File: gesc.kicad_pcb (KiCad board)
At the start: 4 copper layers, 111 x 111 mm, 164 parts, among them J1 Conn_01x06, J10 PHASE_C, J11 PHASE_B, J12 NTC, J13 T-Motor, J14 Conn_01x03, J15 EXT_OFF, J2 Conn_01x06, J3 Conn_01x06, J4 Conn_01x05, J5 Conn_01x03, J6 USB_B_Mini, J7 BAT+, J8 BAT-, J9 PHASE_A, Q1 BSC070N10NS5, Q2 BSC070N10NS5, Q3 BSC070N10NS5, Q4 BSC070N10NS5, Q5 BSC070N10NS5, Q6 BSC070N10NS5, U1 STM32F405RGTx, U10 LM5008MM, U11 SN74LVC1G66DBVR, U12 LM5107, U13 SN74LVC1G66DBVR, U14 AQY282S, U15 LM5107, U16 EYSGJNZWY, U17 LMR12010YMKE_NOPB, U2 SN74LVC1G66DBVR, U3 LM5107, U4 INA240A1, U5 INA240A1, U6 INA240A1, U7 SN74LVC1G66DBVR, U8 SN74LVC1G66DBVR, U9 SN74LVC1G66DBVR, Y1 X50328MSB2GI

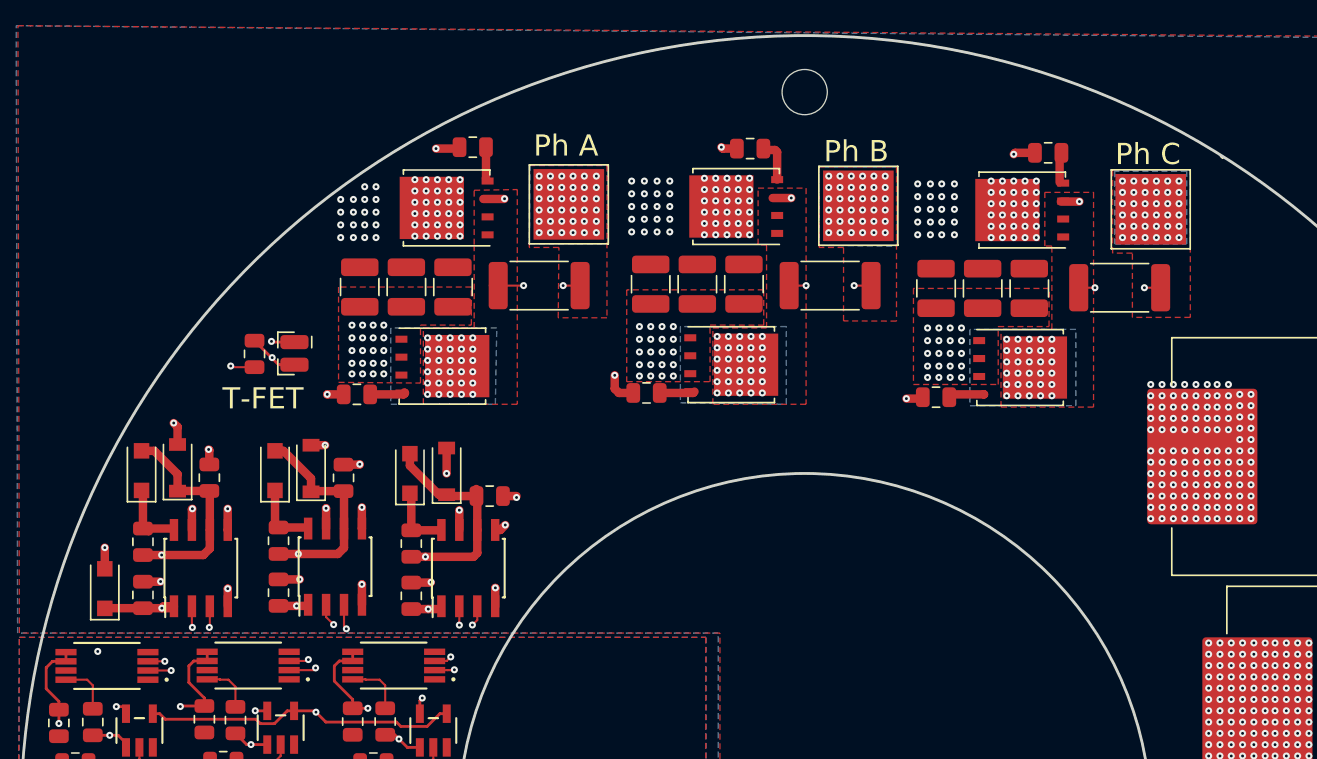
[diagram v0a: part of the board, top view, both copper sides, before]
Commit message: Version mit UCC27211
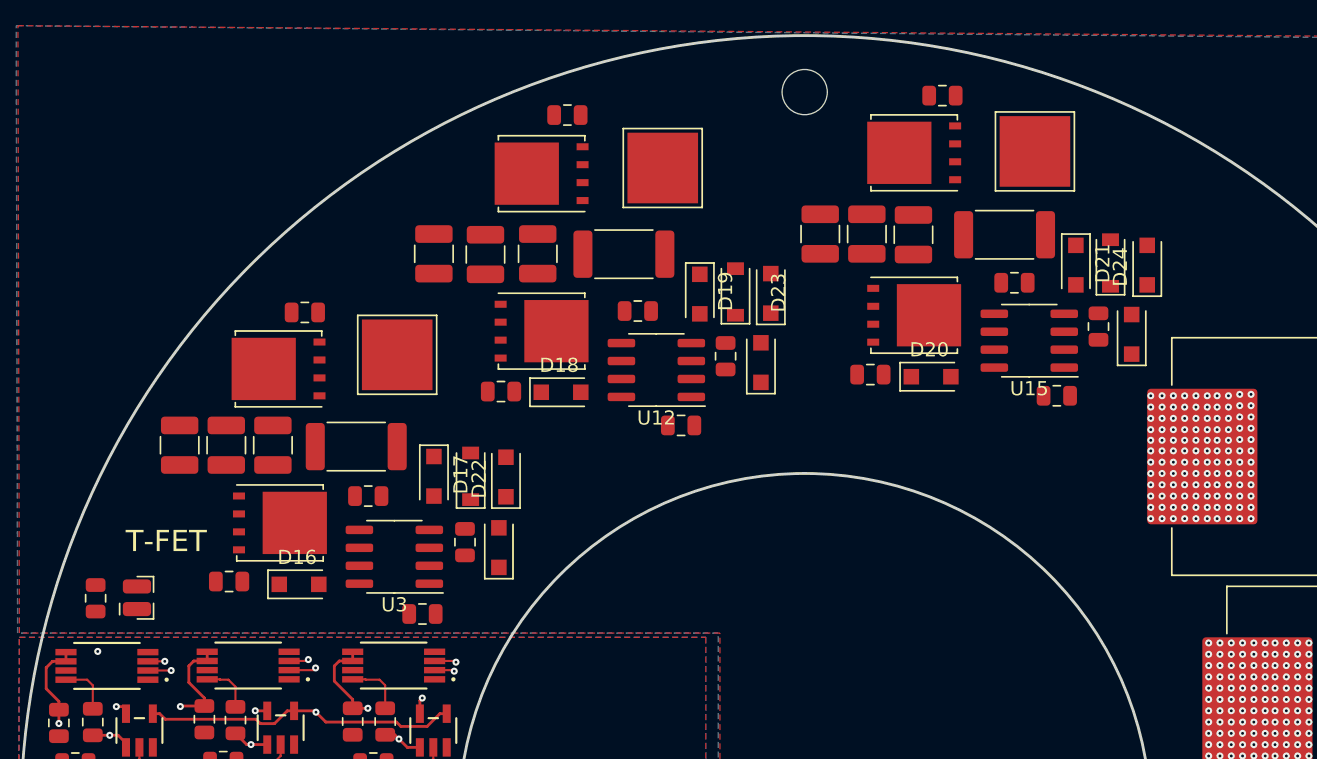
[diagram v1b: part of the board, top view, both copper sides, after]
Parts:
- added D17: SMF14A, Diode_SMD:D_SOD-123F, F.Cu at (73.7, 75.7)
- added D18: SMF14A, Diode_SMD:D_SOD-123F, F.Cu at (82.7, 69.7)
- added D19: SMF14A, Diode_SMD:D_SOD-123F, F.Cu at (92.6, 62.8)
- added D20: SMF14A, Diode_SMD:D_SOD-123F, F.Cu at (108.9, 68.6)
- added D21: SMF14A, Diode_SMD:D_SOD-123F, F.Cu at (119.2, 60.7)
- added D22: SMF58A, Diode_SMD:D_SOD-123F, F.Cu at (78.8, 75.7)
- added D23: SMF58A, Diode_SMD:D_SOD-123F, F.Cu at (97.6, 62.7)
- added D24: SMF58A, Diode_SMD:D_SOD-123F, F.Cu at (124.2, 60.7)
- D16: value SMF12A -> SMF14A
- U12, U15, U3: value LM5107 -> UCC27211
- moved D15 52.0 mm to (123.1, 65.6)
- moved C32 51.0 mm to (120.8, 65.1), turned to 90 degrees
- moved D12 49.3 mm to (121.6, 60.6)
- moved C29 47.8 mm to (117.8, 70.0), turned to 180 degrees
- moved U15 42.9 mm to (115.9, 66.1), turned to 180 degrees
- moved R49 40.1 mm to (114.8, 62.0), turned to 0 degrees
- moved D14 35.2 mm to (96.9, 67.6)
- moved C27 34.2 mm to (94.4, 67.2), turned to 90 degrees
- moved D10 32.5 mm to (95.1, 62.6)
- moved C22 30.9 mm to (91.2, 72.1), turned to 180 degrees
- moved U12 26.7 mm to (89.5, 68.2), turned to 180 degrees
- moved D13 25.9 mm to (78.3, 80.7)
- moved R48 24.0 mm to (88.2, 64.0), turned to 0 degrees
- moved C21 22.8 mm to (75.9, 80.4), turned to 90 degrees
- moved C38 22.1 mm to (73.7, 59.9)
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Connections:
- D16 pad 1: +12V -> /Driver/GL_A
- R13 pad 1: /Driver/SH_A_R -> /Driver/SH_A
- R17 pad 1: /Driver/SH_B_R -> /Driver/SH_B
- R19 pad 1: /Driver/SH_C_R -> /Driver/SH_C
- U12 pad 2: /MCU/H2 -> Net-(C27-Pad1)
- U12 pad 3: /MCU/L2 -> /Driver/GH_B
- U12 pad 4: GND -> /Driver/SH_B_R
- U12 pad 5: /Driver/GL_B -> /MCU/H2
- U12 pad 6: /Driver/SH_B_R -> /MCU/L2
- U12 pad 7: /Driver/GH_B -> GND
- U12 pad 8: Net-(C27-Pad1) -> /Driver/GL_B
- U15 pad 2: /MCU/H3 -> Net-(C32-Pad1)
- U15 pad 3: /MCU/L3 -> /Driver/GH_C
- U15 pad 4: GND -> /Driver/SH_C_R
- U15 pad 5: /Driver/GL_C -> /MCU/H3
- U15 pad 6: /Driver/SH_C_R -> /MCU/L3
- U15 pad 7: /Driver/GH_C -> GND
- U15 pad 8: Net-(C32-Pad1) -> /Driver/GL_C
- U3 pad 2: /MCU/H1 -> Net-(C21-Pad1)
- U3 pad 3: /MCU/L1 -> /Driver/GH_A
- U3 pad 4: GND -> /Driver/SH_A_R
- U3 pad 5: /Driver/GL_A -> /MCU/H1
- U3 pad 6: /Driver/SH_A_R -> /MCU/L1
- U3 pad 7: /Driver/GH_A -> GND
- U3 pad 8: Net-(C21-Pad1) -> /Driver/GL_A
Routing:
- net GND: track 117.4 -> 0.74 mm, vias 390 -> 319
- net /Driver/SH_B: track 104.3 -> 23.6 mm, vias 34 -> 2
- net /Driver/SH_C: track 122.9 -> 46.1 mm, vias 34 -> 2
- net /Driver/SH_A: track 86.7 -> 17.1 mm, vias 34 -> 2
- net /Driver/GH_C: track 56.1 -> 0.00 mm, vias 2 -> 0
- net /POWER/PHASE_B: track 59.0 -> 9.98 mm, vias 38 -> 1
- net /Driver/GH_B: track 45.1 -> 0.00 mm, vias 2 -> 0
- net /POWER/PHASE_A: track 49.5 -> 6.33 mm, vias 38 -> 1
- net /Driver/GH_A: track 36.6 -> 0.00 mm, vias 2 -> 0
- net /POWER/PHASE_C: track 67.0 -> 30.5 mm, vias 38 -> 1
- net /Driver/SH_A_R: track 36.1 -> 0.00 mm, vias 2 -> 0
- net /Driver/SH_B_R: track 35.4 -> 0.00 mm, vias 2 -> 0
- net /Driver/SH_C_R: track 35.3 -> 0.00 mm, vias 2 -> 0
- net /Driver/GL_C: track 34.9 -> 0.00 mm, vias 2 -> 0
- net /MCU/H3: track 27.9 -> 62.2 mm, vias 2 -> 1
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- removed copper zone on B.Cu, net /Driver/SH_A
- removed copper zone on F.Cu, net /Driver/SH_A
- removed copper zone on B.Cu, net /Driver/SH_B
- removed copper zone on F.Cu, net /Driver/SH_B
- removed copper zone on B.Cu, net /Driver/SH_C
- removed copper zone on F.Cu, net /Driver/SH_C
- removed copper zone on B.Cu, net /POWER/PHASE_A
- removed copper zone on F.Cu, net /POWER/PHASE_A
- removed copper zone on B.Cu, net /POWER/PHASE_B
- removed copper zone on F.Cu, net /POWER/PHASE_B
- removed copper zone on B.Cu, net /POWER/PHASE_C
- removed copper zone on F.Cu, net /POWER/PHASE_C
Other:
- net class POWER: trace_width 0.2 -> 0.6
- rule trace_min: 0.1 -> 0.15
- board text removed: "Ph A"
- board text removed: "Ph B"
- board text removed: "Ph C"

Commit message: save
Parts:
- removed D10, D12, D9: MBR2H100SFTN, Diode_SMD:D_SOD-123
- removed D13, D14, D15, D16, D17, D18, D19, D20, D21: SMF14A, Diode_SMD:D_SOD-123F
- removed D22, D23, D24: SMF58A, Diode_SMD:D_SOD-123F
- removed R47, R48, R49: 5r60, Resistor_SMD:R_0805_2012Metric
- U12, U15, U3: value UCC27211 -> 2ED2304S06F
- moved C15 4.48 mm to (68.7, 83.9)
- moved C29 3.31 mm to (114.6, 70.5)
- moved R43 3.17 mm to (81.6, 70.3)
- moved C22 2.58 mm to (89.3, 70.3)
- moved U12 2.53 mm to (91.3, 66.4), turned to 0 degrees
- moved C27 2.51 mm to (96.2, 65.5), turned to 270 degrees
- moved J11 2.30 mm to (92.0, 54.8)
- moved Q5 2.30 mm to (83.5, 55.2)
- moved R42 2.30 mm to (85.3, 51.1)
- moved C38 2.30 mm to (75.8, 60.9)
- moved R46 2.30 mm to (89.3, 60.9)
- moved Q6 2.30 mm to (83.5, 66.4)
- moved C44 2.30 mm to (79.5, 60.9)
- moved C53 2.30 mm to (83.2, 60.9)
- moved R26 2.29 mm to (106.2, 70.2)
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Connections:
- C21 pad 2: /Driver/SH_A_R -> /Driver/SH_A
- C27 pad 2: /Driver/SH_B_R -> /Driver/SH_B
- C32 pad 2: /Driver/SH_C_R -> /Driver/SH_C
- U12 pad 1: +12V -> /MCU/L2
- U12 pad 2: Net-(C27-Pad1) -> /MCU/H2
- U12 pad 3: /Driver/GH_B -> +12V
- U12 pad 4: /Driver/SH_B_R -> GND
- U12 pad 5: /MCU/H2 -> /Driver/GL_B
- U12 pad 6: /MCU/L2 -> /Driver/SH_B
- U12 pad 7: GND -> /Driver/GH_B
- U12 pad 8: /Driver/GL_B -> Net-(C27-Pad1)
- U15 pad 1: +12V -> /MCU/L3
- U15 pad 2: Net-(C32-Pad1) -> /MCU/H3
- U15 pad 3: /Driver/GH_C -> +12V
- U15 pad 4: /Driver/SH_C_R -> GND
- U15 pad 5: /MCU/H3 -> /Driver/GL_C
- U15 pad 6: /MCU/L3 -> /Driver/SH_C
- U15 pad 7: GND -> /Driver/GH_C
- U15 pad 8: /Driver/GL_C -> Net-(C32-Pad1)
- U3 pad 1: +12V -> /MCU/L1
- U3 pad 2: Net-(C21-Pad1) -> /MCU/H1
- U3 pad 3: /Driver/GH_A -> +12V
- U3 pad 4: /Driver/SH_A_R -> GND
- U3 pad 5: /MCU/H1 -> /Driver/GL_A
- U3 pad 6: /MCU/L1 -> /Driver/SH_A
- U3 pad 7: GND -> /Driver/GH_A
- U3 pad 8: /Driver/GL_A -> Net-(C21-Pad1)
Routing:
- net /Driver/SH_C: track 46.1 -> 97.0 mm, vias 2 -> 41
- net /POWER/PHASE_C: track 30.5 -> 58.4 mm, vias 1 -> 51
- net /Driver/GH_C: track 0.00 -> 25.5 mm, vias 0 -> 2
- net /MCU/L3: track 65.5 -> 83.9 mm, vias 1 -> 2
- net /MCU/H3: track 62.2 -> 79.6 mm, vias 1 -> 2
- net /Driver/GL_C: track 0.00 -> 13.0 mm, vias 0 -> 2
- net GND: track 0.74 -> 13.3 mm, vias 319 -> 375
- net +12V: track 126.8 -> 131.3 mm
- net /Driver/SH_A: track 17.1 -> 19.8 mm
- net Net-(C32-Pad1): track 0.00 -> 2.58 mm
- net Net-(Q4-Pad4): track 0.00 -> 2.14 mm
- net Net-(Q3-Pad4): track 0.00 -> 2.14 mm
- net VBAT: vias 318 -> 389
- added copper zone on F.Cu, net /Driver/SH_C
- added copper zone on F.Cu, net /POWER/PHASE_C

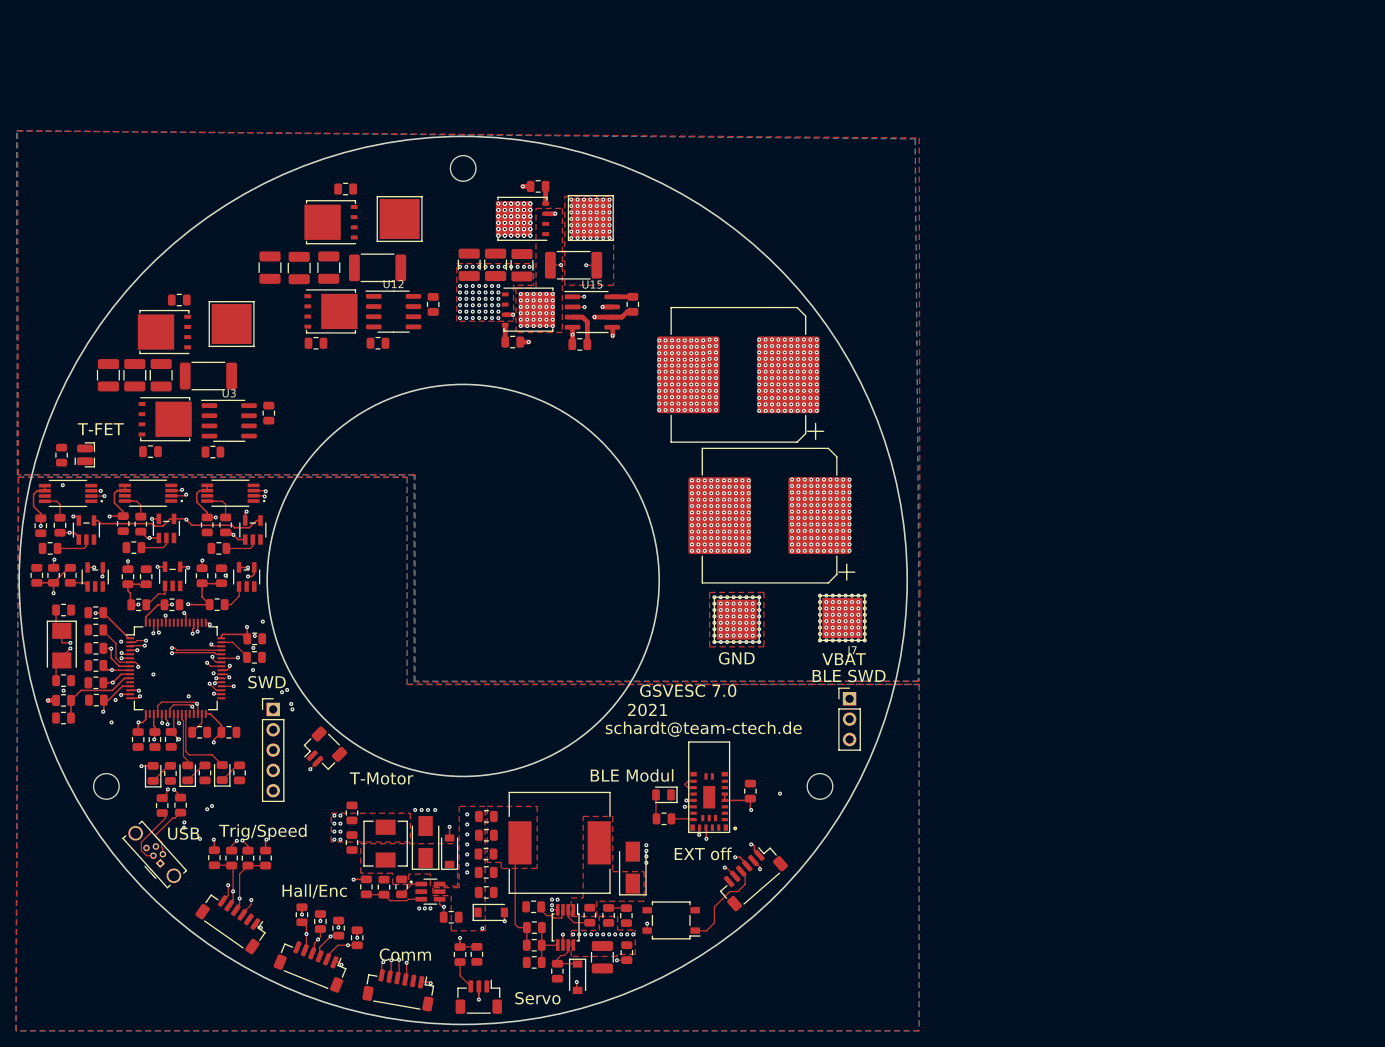
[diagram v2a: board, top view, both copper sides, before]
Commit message: - new driver 2ED2304S06F - separat Elkos for each phase - new FET placement
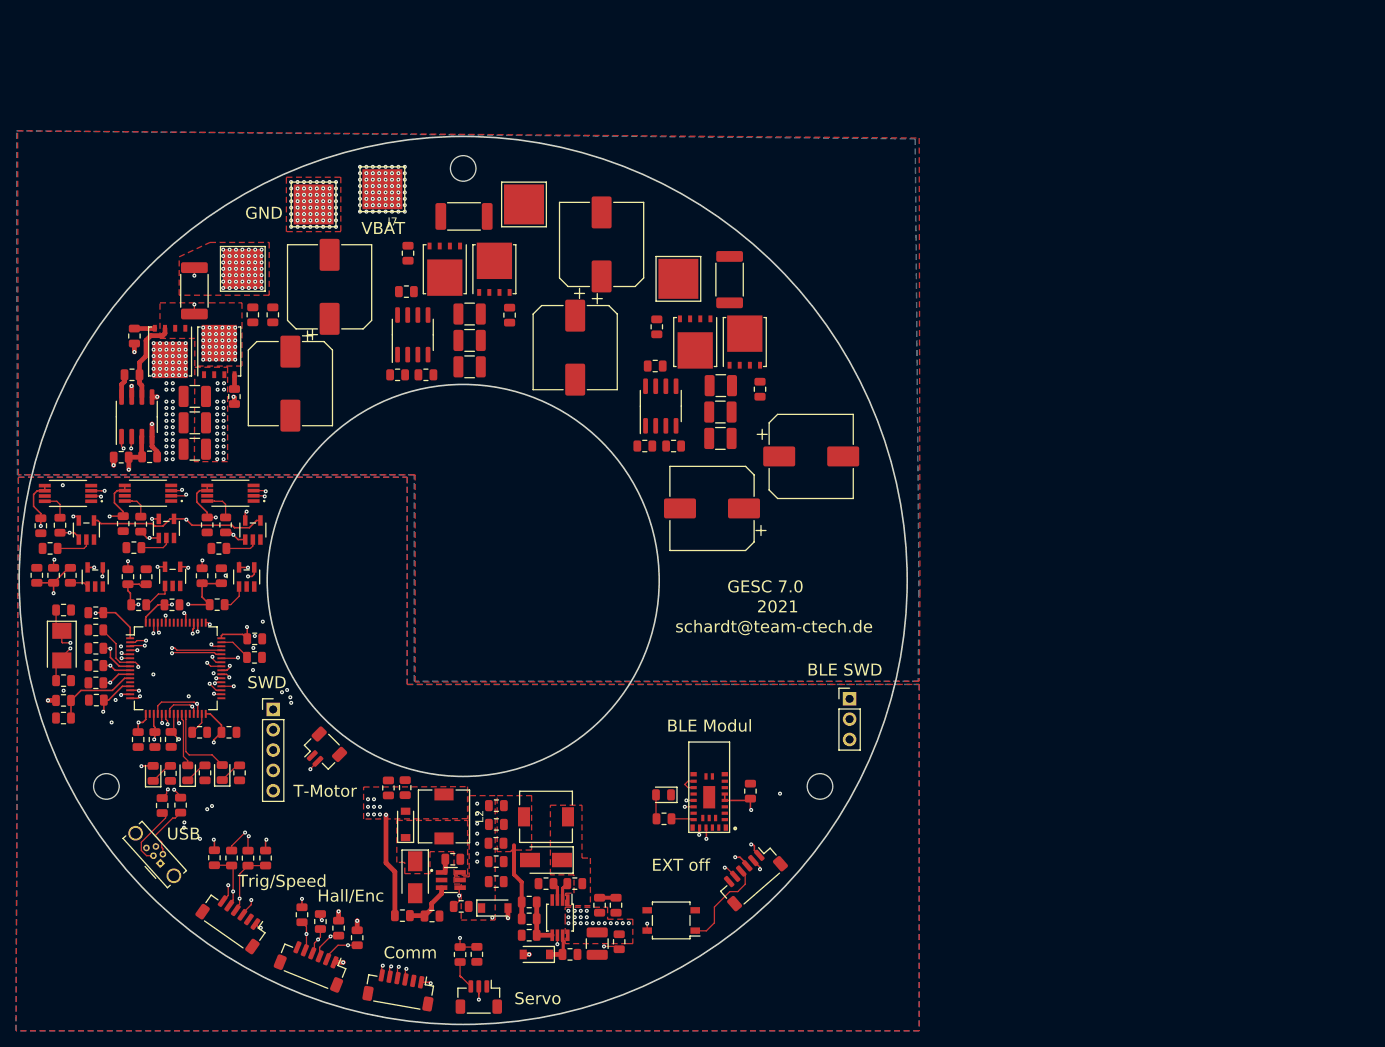
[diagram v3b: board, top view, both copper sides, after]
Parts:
- removed J12: NTC, gesc:2pad_smd_testpin
- added C55: 100n, Capacitor_SMD:C_0805_2012Metric, F.Cu at (60.8, 84.5)
- added C57: 100n, Capacitor_SMD:C_0805_2012Metric, F.Cu at (91.8, 74.3)
- added C58: 100n, Capacitor_SMD:C_0805_2012Metric, F.Cu at (122.7, 83.2)
- added C59: 100u, Capacitor_SMD:CP_Elec_10x10, F.Cu at (114.0, 70.9)
- added C60: 100u, Capacitor_SMD:CP_Elec_10x10, F.Cu at (117.3, 58.0)
- added C61: 100u, Capacitor_SMD:CP_Elec_10x10, F.Cu at (143.5, 84.5)
- added C62: 100u, Capacitor_SMD:CP_Elec_10x10, F.Cu at (131.1, 91.0)
- added R47: CMFB103F3950FANT, Resistor_SMD:R_0805_2012Metric, F.Cu at (73.7, 66.8)
- C54, C56: value 330u -> 100u; footprint Capacitor_SMD:CP_Elec_16x17.5 -> Capacitor_SMD:CP_Elec_10x10
- L1: footprint Inductor_SMD:L_12x12mm_H4.5mm -> Inductor_SMD:L_6.3x6.3_H3
- L2: value 4u70 -> 15u0; footprint Inductor_SMD:L_Sunlord_MWSA0518_5.4x5.2mm -> Inductor_SMD:L_6.3x6.3_H3
- moved J7 78.6 mm to (89.9, 51.1)
- moved J8 74.1 mm to (81.3, 53.0)
- moved C56 62.0 mm to (83.3, 63.3), turned to 90 degrees
- moved C54 56.0 mm to (78.4, 75.4), turned to 270 degrees
- moved C52 38.2 mm to (132.1, 82.2), turned to 0 degrees
- moved C36 33.6 mm to (132.1, 78.9), turned to 0 degrees
- moved R36 31.7 mm to (76.2, 66.8)
- moved R26 31.5 mm to (137.1, 76.1), turned to 270 degrees
- moved C43 29.1 mm to (132.2, 75.6), turned to 0 degrees
- moved Q4 27.4 mm to (135.2, 70.2), turned to 90 degrees
- moved C38 26.6 mm to (100.8, 70.0), turned to 0 degrees
- moved Q3 26.5 mm to (129.0, 70.2), turned to 270 degrees
- moved C44 24.6 mm to (100.8, 73.3), turned to 0 degrees
- moved R43 24.5 mm to (105.8, 66.8), turned to 270 degrees
- moved R25 23.0 mm to (124.2, 68.3), turned to 270 degrees
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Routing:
- net /Driver/SH_C: track 97.0 -> 17.5 mm, vias 41 -> 2
- net /MCU/L3: track 83.9 -> 26.6 mm, vias 2 -> 1
- net /MCU/H3: track 79.6 -> 23.5 mm, vias 2 -> 1
- net /POWER/PHASE_C: track 58.4 -> 3.53 mm, vias 51 -> 1
- net /Driver/SH_A: track 19.8 -> 58.2 mm, vias 2 -> 39
- net /POWER/PHASE_A: track 6.33 -> 35.4 mm, vias 1 -> 51
- net /Driver/GH_C: track 25.5 -> 0.00 mm, vias 2 -> 0
- net /Driver/GL_C: track 13.0 -> 0.00 mm, vias 2 -> 0
- net VCC: track 82.5 -> 94.2 mm, vias 39 -> 38
- net /Driver/GL_A: track 0.00 -> 11.2 mm, vias 0 -> 2
- net GND: track 13.3 -> 5.37 mm, vias 375 -> 90
- net /Driver/GH_A: track 0.00 -> 6.84 mm, vias 0 -> 2
- net +12V: track 131.3 -> 137.0 mm, vias 11 -> 12
- net /MCU/H1: track 35.3 -> 40.5 mm, vias 2 -> 3
- net /MCU/L1: track 42.9 -> 47.0 mm, vias 2 -> 3
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- added copper zone on F.Cu, net /Driver/SH_A
- added copper zone on F.Cu, net /POWER/PHASE_A
- removed copper zone on F.Cu, net /Driver/SH_C
- removed copper zone on F.Cu, net /POWER/PHASE_C
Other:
- board text added: "GESC 7.0"
- board text removed: "GSVESC 7.0"
- board text removed: "T-FET"

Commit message: save
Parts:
- removed C50: 22u0/25V, Capacitor_SMD:C_0805_2012Metric
- removed D8: SS210, Diode_SMD:D_SMA
- removed L2: 15u0, Inductor_SMD:L_6.3x6.3_H3
- added R48: 110k, Resistor_SMD:R_0805_2012Metric, F.Cu at (93.7, 133.2)
- C33: value 100n -> 3n30
- D7: value B5819W -> ZPD12; footprint Diode_SMD:D_SOD-123 -> Diode_SMD:D_MiniMELF
- R15: value 100k -> 110k
- R27: value 11k0 -> 3k30
- R34: value 11k0 -> 330k
- R44: value 33k0 -> 2k10
- U17: value LMR12010YMKE_NOPB -> TPS82140; footprint gesc:SOT95P280X110-6N -> Package_LGA:Texas_SIL0008D_MicroSiP-8-1EP_2.8x3mm_P0.65mm_EP1.1x1.9mm
- moved R25 86.6 mm to (209.4, 83.8), turned to 90 degrees
- moved J10 80.2 mm to (200.0, 95.4)
- moved Q3 77.2 mm to (205.3, 81.9), turned to 90 degrees
- moved C32 71.5 mm to (195.4, 76.5), turned to 270 degrees
- moved R31 71.4 mm to (200.1, 87.7)
- moved C52 68.1 mm to (199.8, 74.5), turned to 180 degrees
- moved C43 67.9 mm to (199.8, 81.6), turned to 180 degrees
- moved C36 67.7 mm to (199.8, 78.1), turned to 180 degrees
- moved C61 66.6 mm to (207.9, 67.5), turned to 90 degrees
- moved U15 65.5 mm to (190.2, 77.5), turned to 0 degrees
- moved C62 65.0 mm to (191.5, 67.1), turned to 270 degrees
- moved C58 62.8 mm to (184.9, 74.8), turned to 90 degrees
- moved Q4 61.0 mm to (194.3, 85.4), turned to 270 degrees
- moved C29 59.1 mm to (185.2, 78.7), turned to 270 degrees
- moved C22 55.2 mm to (146.7, 54.3)
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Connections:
- C33 pad 2: Net-(C33-Pad2) -> GND
- D7 pad 1: Net-(C33-Pad2) -> /Driver/V_AUX
- D7 pad 2: VCC -> GND
- J15 pad 4: /Driver/EN_3V3 -> /Driver/V_AUX
- R12 pad 1: /Driver/EN_12V -> Net-(R12-Pad1)
- R27 pad 1: +12V -> /Driver/V_AUX
- R27 pad 2: Net-(R27-Pad2) -> VBAT
- R34 pad 1: GND -> VCC
- R44 pad 1: VCC -> /Driver/V_AUX
- R44 pad 2: Net-(R34-Pad2) -> /Driver/EN_12V
- U10 pad 6: /Driver/EN_12V -> Net-(R12-Pad1)
- U14 pad 1: /Driver/EN_3V3 -> /Driver/EN_12V
- U14 pad 4: Net-(R27-Pad2) -> Net-(R12-Pad1)
- U17 pad 1: Net-(C33-Pad1) -> (no net)
- U17 pad 2: GND -> +12V
- U17 pad 3: Net-(R34-Pad2) -> GND
- U17 pad 4: Net-(R27-Pad2) -> VCC
- U17 pad 5: +12V -> VCC
- U17 pad 6: Net-(C33-Pad2) -> Net-(R34-Pad2)
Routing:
- net Net-(R27-Pad2): track 28.9 -> 0.00 mm, vias 2 -> 0
- net /Driver/EN_12V: track 30.0 -> 13.7 mm, vias 3 -> 1
- net /Driver/V_AUX: track 0.00 -> 15.0 mm
- net Net-(R12-Pad1): track 0.00 -> 14.1 mm, vias 0 -> 2
- net VCC: track 94.2 -> 80.4 mm, vias 38 -> 36
- net VBUS: track 50.0 -> 37.2 mm
- net /Driver/EN_3V3: track 10.9 -> 0.00 mm
- net +12V: track 137.0 -> 141.6 mm
- net VBAT: track 88.2 -> 92.0 mm
- net Net-(R34-Pad2): track 6.28 -> 3.98 mm
- net /MCU/TEMP_MOTOR: track 52.6 -> 50.3 mm
- net /MCU/SERVO: track 66.7 -> 68.7 mm
- net GND: vias 90 -> 93
- removed copper zone on F.Cu, net Net-(C33-Pad2)
